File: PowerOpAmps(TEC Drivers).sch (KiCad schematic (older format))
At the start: 23 parts, among them U301 OPA569AIDWPR, U302 OPA569AIDWPR

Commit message: SOLVED: GND and 4.2V
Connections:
- net GND: now also C305.2, U301.13 (V+)
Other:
- moved on the sheet: C307
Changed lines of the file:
@@
 	7500 2500 7500 2400
 Wire Wire Line
-	7500 2600 7600 2600
-Wire Wire Line
-	8000 2600 8000 2700
-Wire Wire Line
-	8000 2600 8250 2600
-Connection ~ 8000 2600
+	7850 2600 7850 2700
 $Comp
 L power:GND #PWR0310
 U 1 1 60C9E215
-P 8000 3000
-F 0 "#PWR0310" H 8000 2750 50  0001 C CNN
-F 1 "GND" H 8005 2827 50  0000 C CNN
-F 2 "" H 8000 3000 50  0001 C CNN
-F 3 "" H 8000 3000 50  0001 C CNN
-	1    8000 3000
+P 7850 3000
+F 0 "#PWR0310" H 7850 2750 50  0001 C CNN
+F 1 "GND" H 7855 2827 50  0000 C CNN
+F 2 "" H 7850 3000 50  0001 C CNN
+F 3 "" H 7850 3000 50  0001 C CNN
+	1    7850 3000
 	1    0    0    -1
 $EndComp
@@
 L Device:C C307
 U 1 1 60C9E72B
-P 8000 2850
-F 0 "C307" H 7700 2900 50  0000 L CNN
-F 1 "0.1u" H 7700 2800 50  0000 L CNN
-F 2 "Capacitor_SMD:C_0402_1005Metric" H 8038 2700 50  0001 C CNN
-F 3 "~" H 8000 2850 50  0001 C CNN
-	1    8000 2850
-	1    0    0    -1
-$EndComp
-Connection ~ 8000 2700
+P 7850 2850
+F 0 "C307" H 7550 2900 50  0000 L CNN
+F 1 "0.1u" H 7550 2800 50  0000 L CNN
+F 2 "Capacitor_SMD:C_0402_1005Metric" H 7888 2700 50  0001 C CNN
+F 3 "~" H 7850 2850 50  0001 C CNN
+	1    7850 2850
+	1    0    0    -1
+$EndComp
+Connection ~ 7850 2700
 $Comp
 L power:GND #PWR0308
@@
 	1    0    0    -1
 $EndComp
-$Comp
-L Device:C C305
-U 1 1 60CA0405
-P 7750 2600
-F 0 "C305" V 7600 2500 50  0000 L CNN
-F 1 "100u" V 7700 2650 50  0000 L CNN
-F 2 "Capacitor_SMD:C_0402_1005Metric" H 7788 2450 50  0001 C CNN
-F 3 "~" H 7750 2600 50  0001 C CNN
-	1    7750 2600
-	0    1    1    0
-$EndComp
-Wire Wire Line
-	7900 2600 8000 2600
 Wire Wire Line
 	8250 2600 8250 2800
@@
 	8900 2700 9450 2700
 Wire Wire Line
-	8000 2700 8900 2700
+	7850 2700 8900 2700
 Connection ~ 8900 2700
 Wire Wire Line
@@
 Connection ~ 7650 2700
 Wire Wire Line
-	7650 2700 8000 2700
+	7650 2700 7850 2700
 Wire Wire Line
 	8750 2200 8150 2200
@@
 Text GLabel 7650 1100 2    50   Output ~ 0
 To_Arduino_AtoD_Neg
+$Comp
+L Device:C C305
+U 1 1 60CEBDD3
+P 8050 2600
+F 0 "C305" V 7900 2500 50  0000 L CNN
+F 1 "100u" V 8000 2650 50  0000 L CNN
+F 2 "Capacitor_SMD:C_0402_1005Metric" H 8088 2450 50  0001 C CNN
+F 3 "~" H 8050 2600 50  0001 C CNN
+	1    8050 2600
+	0    1    1    0
+$EndComp
+Wire Wire Line
+	7500 2600 7850 2600
+Wire Wire Line
+	7900 2600 7850 2600
+Connection ~ 7850 2600
+Wire Wire Line
+	8250 2600 8200 2600
 $EndSCHEMATC

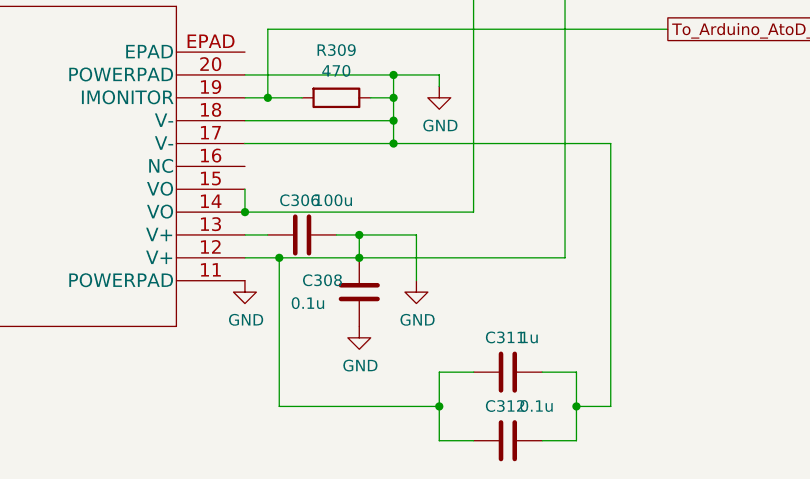
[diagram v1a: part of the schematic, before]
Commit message: changed second 4.2V to GND short in pwropAmps
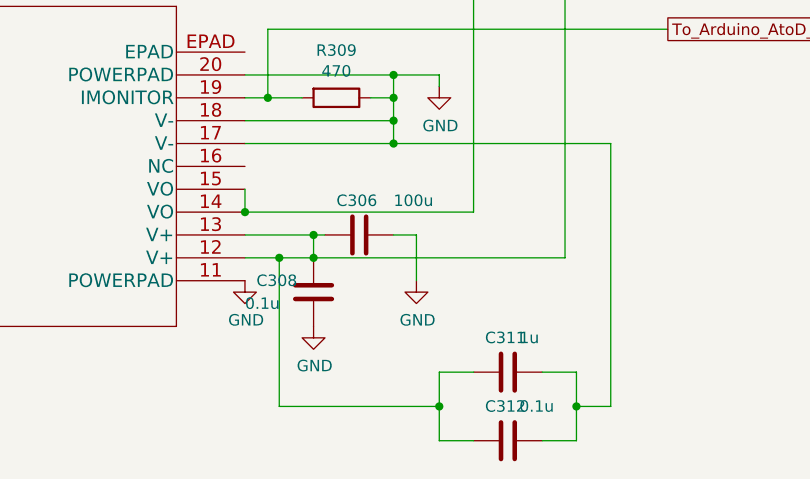
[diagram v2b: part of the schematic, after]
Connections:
- net GND: no longer C305.2, C307.1, C308.1, C309.2, C310.2, C311.2, C312.2, U301.12 (V+), U301.13 (V+), U302.12 (V+)
- net 4.2V: now reaches C306.2, U302.13 (V+)
- net 4.2V: now also C305.2, C307.1, C308.1, C309.2, C310.2, C311.2, C312.2, U301.12 (V+), U301.13 (V+), U302.12 (V+)
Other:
- moved on the sheet: C308
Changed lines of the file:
@@
 $EndComp
 Wire Wire Line
-	7500 5350 7600 5350
-Wire Wire Line
-	8000 5350 8000 5450
-Wire Wire Line
-	8000 5350 8250 5350
-Connection ~ 8000 5350
+	7800 5350 7800 5450
 $Comp
 L power:GND #PWR0311
 U 1 1 60C89B9A
-P 8000 5750
-F 0 "#PWR0311" H 8000 5500 50  0001 C CNN
-F 1 "GND" H 8005 5577 50  0000 C CNN
-F 2 "" H 8000 5750 50  0001 C CNN
-F 3 "" H 8000 5750 50  0001 C CNN
-	1    8000 5750
+P 7800 5750
+F 0 "#PWR0311" H 7800 5500 50  0001 C CNN
+F 1 "GND" H 7805 5577 50  0000 C CNN
+F 2 "" H 7800 5750 50  0001 C CNN
+F 3 "" H 7800 5750 50  0001 C CNN
+	1    7800 5750
 	1    0    0    -1
 $EndComp
@@
 L Device:C C308
 U 1 1 60C89BAE
-P 8000 5600
-F 0 "C308" H 7750 5650 50  0000 L CNN
-F 1 "0.1u" H 7700 5550 50  0000 L CNN
-F 2 "Capacitor_SMD:C_0402_1005Metric" H 8038 5450 50  0001 C CNN
-F 3 "~" H 8000 5600 50  0001 C CNN
-	1    8000 5600
-	1    0    0    -1
-$EndComp
-Connection ~ 8000 5450
-$Comp
-L Device:C C306
-U 1 1 60C89BB9
-P 7750 5350
-F 0 "C306" V 7600 5250 50  0000 L CNN
-F 1 "100u" V 7600 5400 50  0000 L CNN
-F 2 "Capacitor_SMD:C_0402_1005Metric" H 7788 5200 50  0001 C CNN
-F 3 "~" H 7750 5350 50  0001 C CNN
-	1    7750 5350
-	0    1    1    0
-$EndComp
-Wire Wire Line
-	7900 5350 8000 5350
+P 7800 5600
+F 0 "C308" H 7550 5650 50  0000 L CNN
+F 1 "0.1u" H 7500 5550 50  0000 L CNN
+F 2 "Capacitor_SMD:C_0402_1005Metric" H 7838 5450 50  0001 C CNN
+F 3 "~" H 7800 5600 50  0001 C CNN
+	1    7800 5600
+	1    0    0    -1
+$EndComp
+Connection ~ 7800 5450
 Wire Wire Line
 	8250 5350 8250 5550
@@
 Connection ~ 8900 2700
 Wire Wire Line
-	8000 5450 8900 5450
+	7800 5450 8900 5450
 Wire Wire Line
 	8900 5450 8900 2700
@@
 Connection ~ 7650 5450
 Wire Wire Line
-	7650 5450 8000 5450
+	7650 5450 7800 5450
 $Comp
 L Device:C C311
@@
 Wire Wire Line
 	8250 2600 8200 2600
+$Comp
+L Device:C C306
+U 1 1 60D0719E
+P 8000 5350
+F 0 "C306" V 7850 5250 50  0000 L CNN
+F 1 "100u" V 7850 5500 50  0000 L CNN
+F 2 "Capacitor_SMD:C_0402_1005Metric" H 8038 5200 50  0001 C CNN
+F 3 "~" H 8000 5350 50  0001 C CNN
+	1    8000 5350
+	0    1    1    0
+$EndComp
+Wire Wire Line
+	7800 5350 7850 5350
+Wire Wire Line
+	7500 5350 7800 5350
+Connection ~ 7800 5350
+Wire Wire Line
+	8150 5350 8250 5350
 $EndSCHEMATC

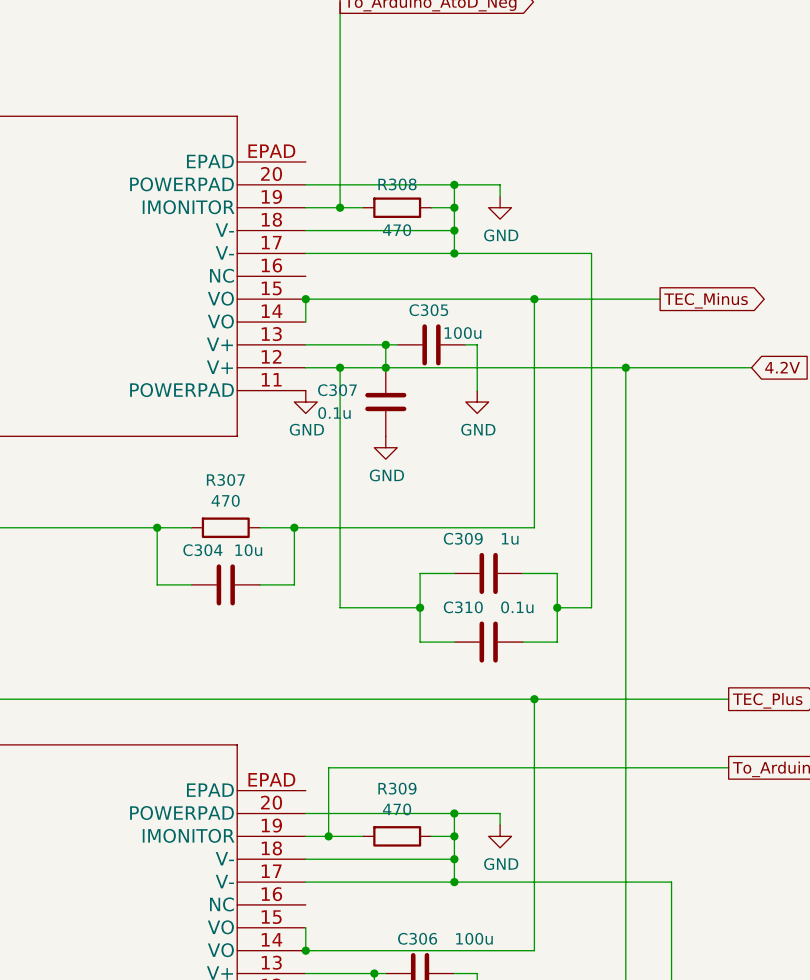
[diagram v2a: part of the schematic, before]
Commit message: grounded all other epads
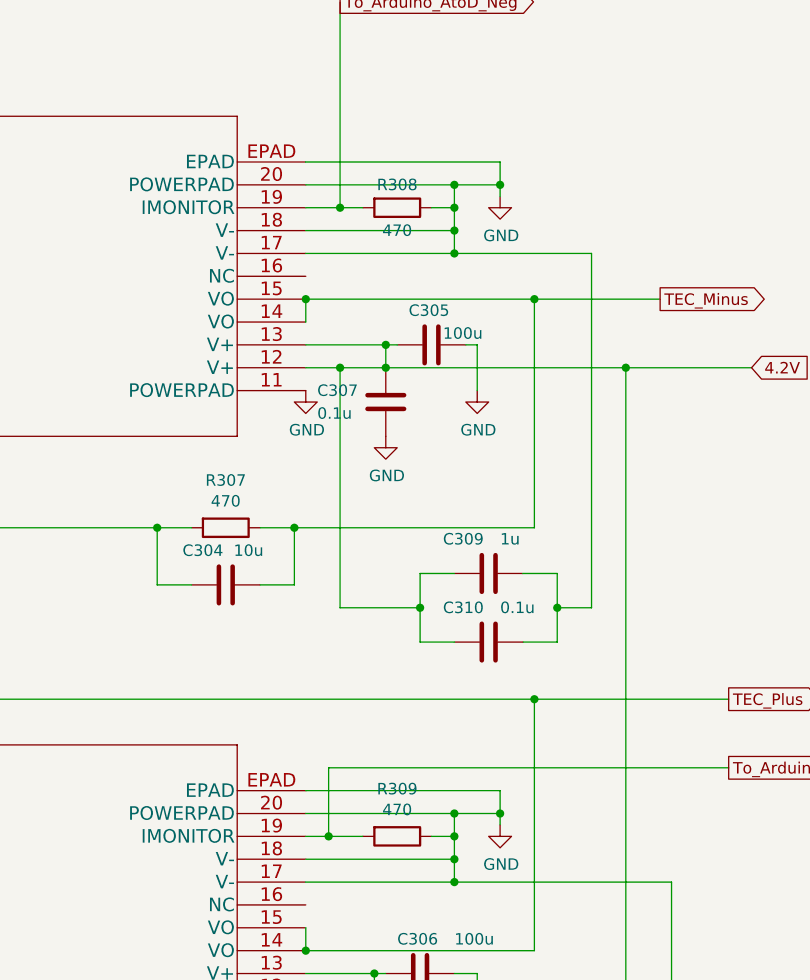
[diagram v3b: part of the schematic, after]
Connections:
- net GND: now also U301.EPAD, U302.EPAD
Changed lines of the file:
@@
 Wire Wire Line
 	8150 5350 8250 5350
+Wire Wire Line
+	7500 1800 8350 1800
+Wire Wire Line
+	8350 1800 8350 1900
+Connection ~ 8350 1900
+Wire Wire Line
+	7500 4550 8350 4550
+Wire Wire Line
+	8350 4550 8350 4650
+Connection ~ 8350 4650
 $EndSCHEMATC

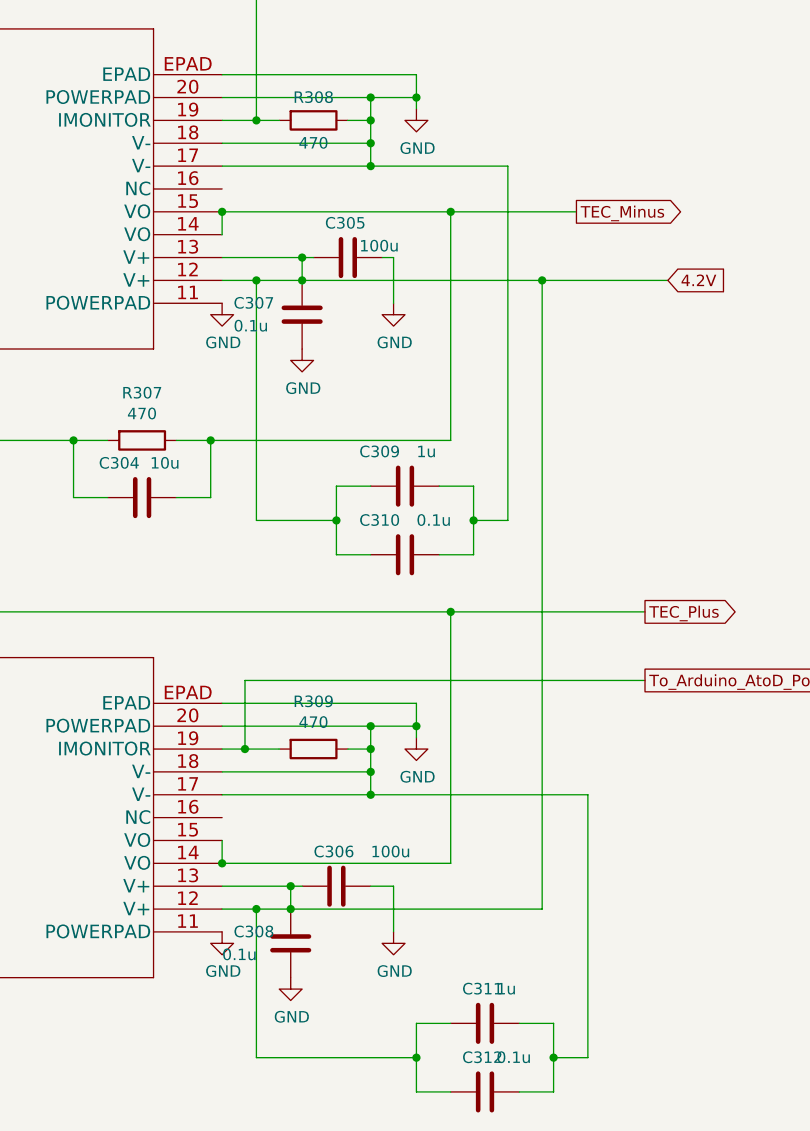
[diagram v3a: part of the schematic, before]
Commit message: update power op amps sch
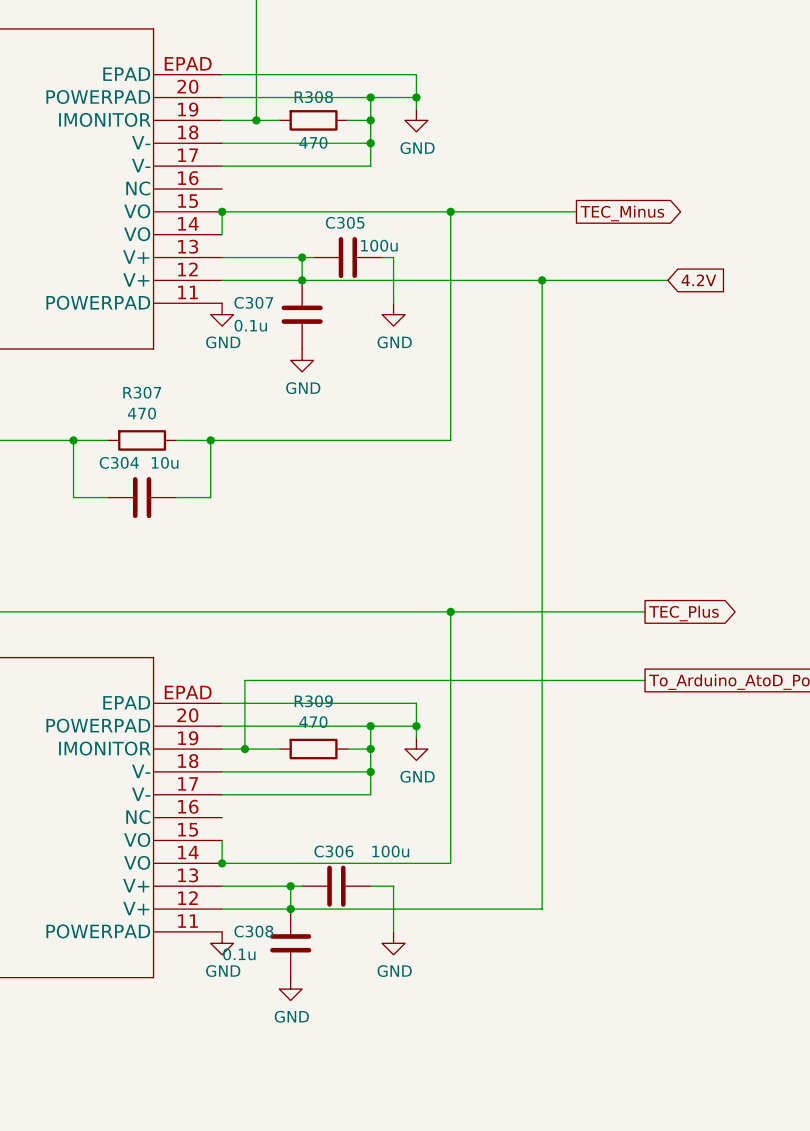
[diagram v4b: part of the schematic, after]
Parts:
- removed C309, C311: 1u, Capacitor_SMD:C_0402_1005Metric, symbol Device:C
- removed C310, C312: 0.1u, Capacitor_SMD:C_0402_1005Metric, symbol Device:C
- C305, C306: footprint Capacitor_SMD:C_0402_1005Metric -> Capacitor_SMD:C_1210_3225Metric
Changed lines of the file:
@@
 Connection ~ 8500 4150
-Wire Wire Line
-	7500 5450 7650 5450
-Wire Wire Line
-	7650 5450 7650 6100
-Wire Wire Line
-	7650 6100 8350 6100
-Wire Wire Line
-	8350 6100 8350 5950
-Wire Wire Line
-	8350 5950 8500 5950
-Connection ~ 7650 5450
-Wire Wire Line
-	7650 5450 7800 5450
-$Comp
-L Device:C C311
-U 1 1 60CD3EBB
-P 8650 5950
-F 0 "C311" V 8500 5850 50  0000 L CNN
-F 1 "1u" V 8500 6000 50  0000 L CNN
-F 2 "Capacitor_SMD:C_0402_1005Metric" H 8688 5800 50  0001 C CNN
-F 3 "~" H 8650 5950 50  0001 C CNN
-	1    8650 5950
-	0    1    1    0
-$EndComp
-$Comp
-L Device:C C312
-U 1 1 60CD4799
-P 8650 6250
-F 0 "C312" V 8500 6150 50  0000 L CNN
-F 1 "0.1u" V 8500 6300 50  0000 L CNN
-F 2 "Capacitor_SMD:C_0402_1005Metric" H 8688 6100 50  0001 C CNN
-F 3 "~" H 8650 6250 50  0001 C CNN
-	1    8650 6250
-	0    1    1    0
-$EndComp
-Wire Wire Line
-	8500 6250 8350 6250
-Wire Wire Line
-	8350 6250 8350 6100
-Connection ~ 8350 6100
-Wire Wire Line
-	8800 6250 8950 6250
-Wire Wire Line
-	8950 6250 8950 6100
-Wire Wire Line
-	8950 6100 9100 6100
-Wire Wire Line
-	9100 6100 9100 4950
-Wire Wire Line
-	9100 4950 8150 4950
-Connection ~ 8150 4950
-Wire Wire Line
-	8800 5950 8950 5950
-Wire Wire Line
-	8950 5950 8950 6100
-Connection ~ 8950 6100
-Wire Wire Line
-	8000 3750 8000 3600
-Wire Wire Line
-	8000 3600 8150 3600
-$Comp
-L Device:C C309
-U 1 1 60CDE792
-P 8300 3600
-F 0 "C309" V 8150 3400 50  0000 L CNN
-F 1 "1u" V 8150 3650 50  0000 L CNN
-F 2 "Capacitor_SMD:C_0402_1005Metric" H 8338 3450 50  0001 C CNN
-F 3 "~" H 8300 3600 50  0001 C CNN
-	1    8300 3600
-	0    1    1    0
-$EndComp
-$Comp
-L Device:C C310
-U 1 1 60CDE79C
-P 8300 3900
-F 0 "C310" V 8150 3700 50  0000 L CNN
-F 1 "0.1u" V 8150 3950 50  0000 L CNN
-F 2 "Capacitor_SMD:C_0402_1005Metric" H 8338 3750 50  0001 C CNN
-F 3 "~" H 8300 3900 50  0001 C CNN
-	1    8300 3900
-	0    1    1    0
-$EndComp
-Wire Wire Line
-	8150 3900 8000 3900
-Wire Wire Line
-	8000 3900 8000 3750
-Connection ~ 8000 3750
-Wire Wire Line
-	8450 3900 8600 3900
-Wire Wire Line
-	8600 3900 8600 3750
-Wire Wire Line
-	8600 3750 8750 3750
-Wire Wire Line
-	8450 3600 8600 3600
-Wire Wire Line
-	8600 3600 8600 3750
-Connection ~ 8600 3750
-Wire Wire Line
-	7650 3750 7650 2700
-Wire Wire Line
-	7500 2700 7650 2700
-Wire Wire Line
-	7650 3750 8000 3750
-Connection ~ 7650 2700
-Wire Wire Line
-	7650 2700 7850 2700
-Wire Wire Line
-	8750 2200 8150 2200
-Wire Wire Line
-	8750 2200 8750 3750
-Connection ~ 8150 2200
 Wire Wire Line
 	3200 1800 3400 1800
@@
 F 0 "C305" V 7900 2500 50  0000 L CNN
 F 1 "100u" V 8000 2650 50  0000 L CNN
-F 2 "Capacitor_SMD:C_0402_1005Metric" H 8088 2450 50  0001 C CNN
+F 2 "Capacitor_SMD:C_1210_3225Metric" H 8088 2450 50  0001 C CNN
 F 3 "~" H 8050 2600 50  0001 C CNN
 	1    8050 2600
@@
 F 0 "C306" V 7850 5250 50  0000 L CNN
 F 1 "100u" V 7850 5500 50  0000 L CNN
-F 2 "Capacitor_SMD:C_0402_1005Metric" H 8038 5200 50  0001 C CNN
+F 2 "Capacitor_SMD:C_1210_3225Metric" H 8038 5200 50  0001 C CNN
 F 3 "~" H 8000 5350 50  0001 C CNN
 	1    8000 5350
@@
 	8350 4550 8350 4650
 Connection ~ 8350 4650
+Wire Wire Line
+	7500 2700 7850 2700
+Wire Wire Line
+	7500 5450 7800 5450
 $EndSCHEMATC
